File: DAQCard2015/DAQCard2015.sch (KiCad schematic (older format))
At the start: 0 parts

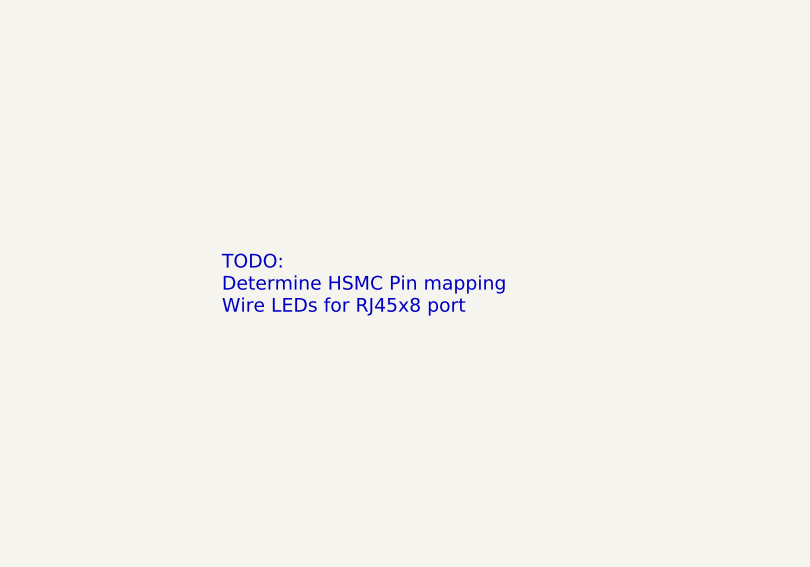
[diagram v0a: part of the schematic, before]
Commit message: Update V1.0 of DAQ Board Includes LED Driver for RJ45 Port, repositioning of JTAG
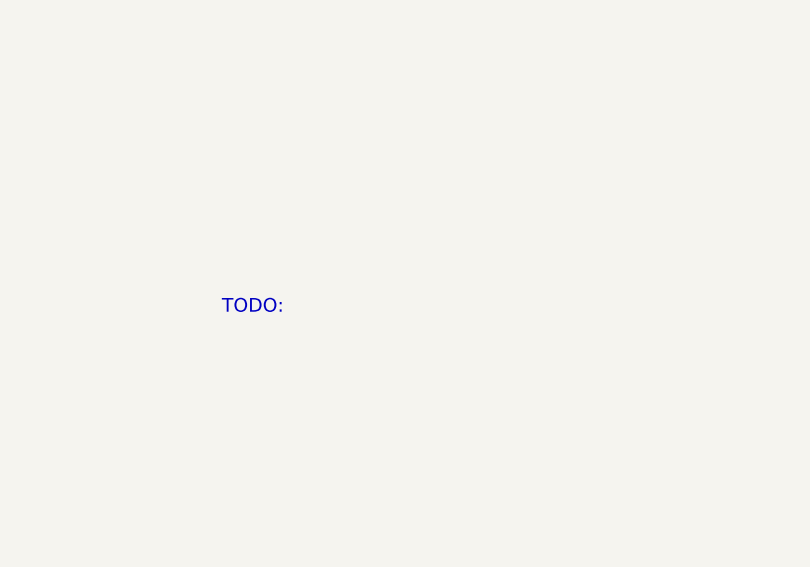
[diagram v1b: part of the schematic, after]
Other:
- note added: "TODO:"
- note removed: "TODO:\nDetermine HSMC Pin mapping\nWire LEDs for RJ45x8 port"
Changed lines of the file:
@@
 	3800 3650 4550 3650
 Text Notes 14100 9250 0    60   ~ 0
-TODO:\nDetermine HSMC Pin mapping\nWire LEDs for RJ45x8 port
+TODO:
 Wire Wire Line
 	3800 3850 4550 3850

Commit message: annotates parts for new build-management tool
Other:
- note added: "TODO:\nHook up HV\nExtend pads on HSMC connectors\nExtend pads on 5V regulator"
- note removed: "TODO:"
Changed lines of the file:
@@
 EESchema Schematic File Version 2
+LIBS:DAQCard2015-rescue
 LIBS:power
 LIBS:device
@@
 	3800 3650 4550 3650
 Text Notes 14100 9250 0    60   ~ 0
-TODO:
+TODO:\nHook up HV\nExtend pads on HSMC connectors\nExtend pads on 5V regulator
 Wire Wire Line
 	3800 3850 4550 3850
